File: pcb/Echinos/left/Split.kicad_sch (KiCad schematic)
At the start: 44 parts, among them J200 USB_B_Micro, J201 Conn_01x04_Socket, J202 Conn_01x12_Socket, J203 Conn_01x06_Socket, J204 Conn_01x06_Socket, J205 Conn_01x06_Socket, J206 USB_C_Receptacle_USB2.0, J207 Conn_01x05_Socket, U202 USBLC6-2P6, U203 74LVC1T45, U204 USBLC6-2P6, U205 XC6210B332MR-G

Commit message: 💥 [PCB] - Split schematic for left and right halves.   - Required to create a common PCB to lower the manufacturing cost
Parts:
- renumbered C222 to C122, C223 to C123, C224 to C124, D231 to D131, D232 to D132, F200 to F100, F201 to F101, FB200 to FB100, H200 to H100, H201 to H101, H202 to H102, H203 to H103, H204 to H104, H205 to H105, J200 to J100, J201 to J101, J202 to J102, J203 to J103, J204 to J104, J205 to J105, J206 to J106, J207 to J107, JP200 to JP100, JP201 to JP101, JP202 to JP102, JP203 to JP103, JP204 to JP104, JP205 to JP105, JP206 to JP106, JP207 to JP107, R206 to R106, R207 to R107, R208 to R108, R209 to R109, R210 to R110, R211 to R111, R212 to R112, R213 to R113, R214 to R114, U202 to U102, U203 to U103, U204 to U104, U205 to U105

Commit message: 💥 [PCB] - Group left and right on the same PCB.   - Schematics are different for each side   - Split trace naming to avoid mixing right and left   - Add mouse bite between both halves to make manufacturing easier (new footprint)
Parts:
- renumbered A1 to A100
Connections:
- net +3.3V renamed +3V3_L
- net +5V renamed +5V_L
- net GND renamed GND_L
- net P_RX renamed RX_split_L
- net P_TX renamed TX_split_L
- net VBUS_split renamed VBUS_split_L
- net col1 renamed col1_L
- net col2 renamed col2_L
- net col3 renamed col3_L
- net col4 renamed col4_L
- net col5 renamed col5_L
- net col6 renamed col6_L
- net row6 renamed row6_L
- net row7 renamed row7_L
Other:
- sheet Backlight ports: added +5V; removed none
- sheet RP2040 ports: added +1V1; removed none

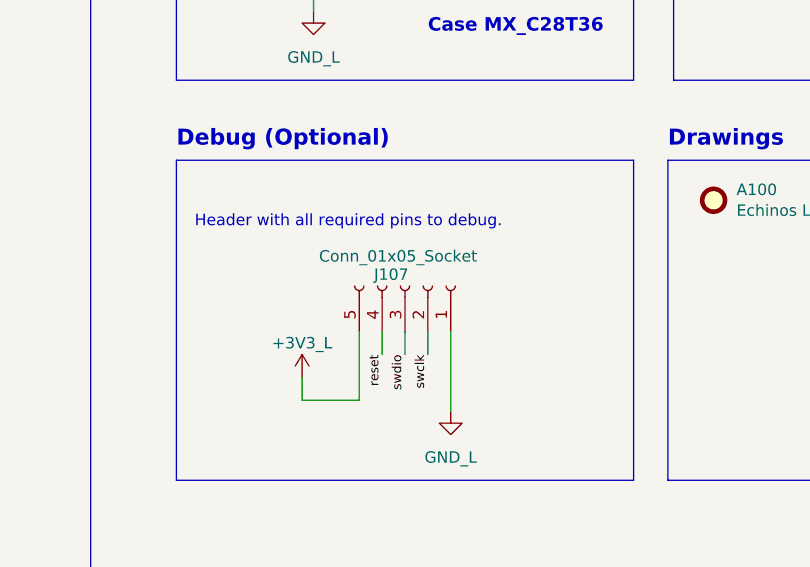
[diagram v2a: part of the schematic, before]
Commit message: 💄 [PCB] - Please DRC at RP2040 level with at least 2 connections on each via for thermal relief. Flip Debug connector to avoid match convention used for pin 1 (squared one) the same as for split connector breakout connectors (power on both).
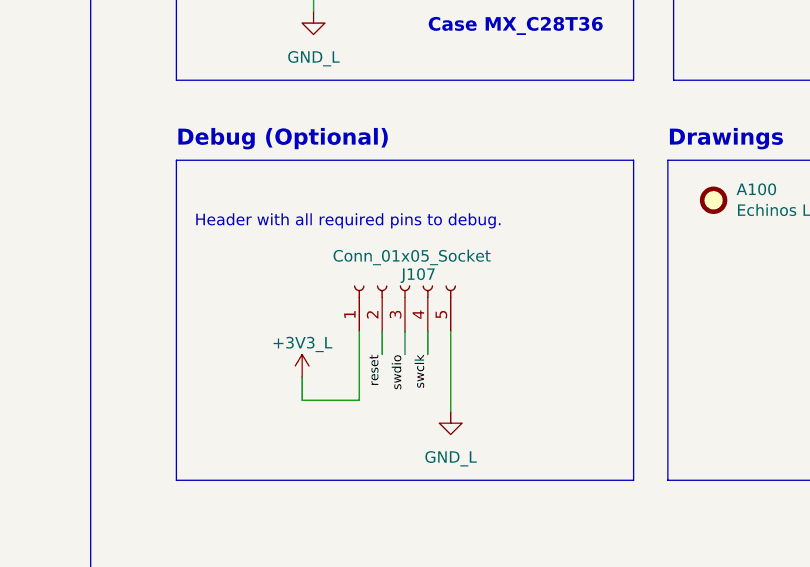
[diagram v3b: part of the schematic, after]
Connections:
- net +3V3_L: now also J107.1 (Pin_1); no longer J107.5 (Pin_5)
- net GND_L: now also J107.5 (Pin_5); no longer J107.1 (Pin_1)
- net reset: now also J107.2 (Pin_2); no longer J107.4 (Pin_4)
- net swclk: now also J107.4 (Pin_4); no longer J107.2 (Pin_2)
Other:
- moved on the sheet: J107
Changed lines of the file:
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@@
 	(symbol
 		(lib_id "Connector:Conn_01x05_Socket")
-		(at 325.12 222.25 270)
-		(mirror x)
+		(at 325.12 222.25 90)
 		(unit 1)
 		(body_style 1)
@@
 		(dnp no)
 		(property "Reference" "J107"
-			(at 323.596 220.98 90)
+			(at 326.644 220.98 90)
 			(show_name no)
 			(do_not_autoplace no)
@@
 		)
 		(property "Value" "Conn_01x05_Socket"
-			(at 324.358 218.948 90)
+			(at 325.882 218.948 90)
 			(show_name no)
 			(do_not_autoplace no)
